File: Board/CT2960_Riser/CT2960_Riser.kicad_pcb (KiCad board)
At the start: 2 copper layers, 105 x 150 mm, 65 parts, among them IC1 74LVC8T245, IC2 74LVC8T245, IC3 74LVC8T245, IC4 74LVC8T245, IC5 74LVC8T245, IC6 74LVC8T245, J1 Conn_02x20_Odd_Even, J2 Conn_02x12_Top_Bottom, J3 Bus_ISA_16bit, J4 Conn_02x20_Odd_Even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

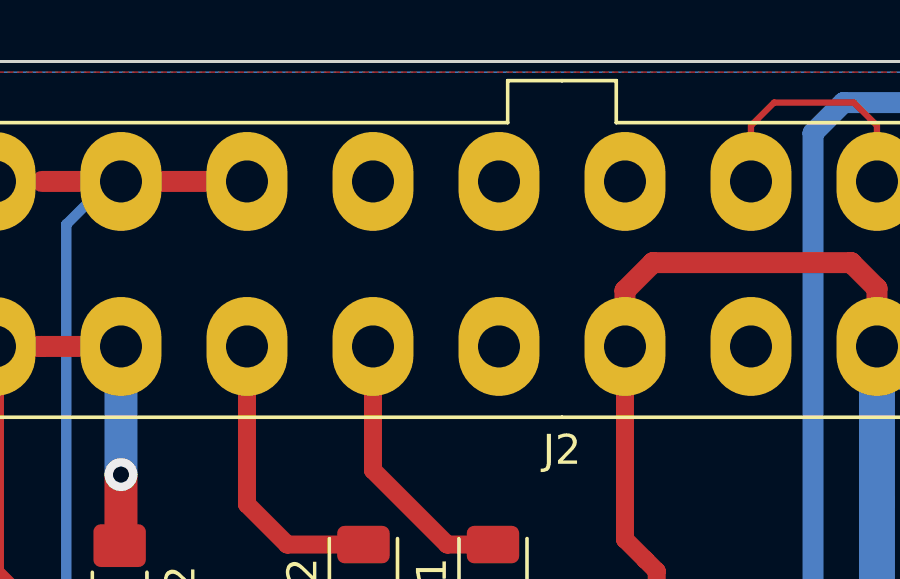
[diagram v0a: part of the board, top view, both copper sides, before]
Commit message: Fixed DRC from reporting unconnected trace/pad
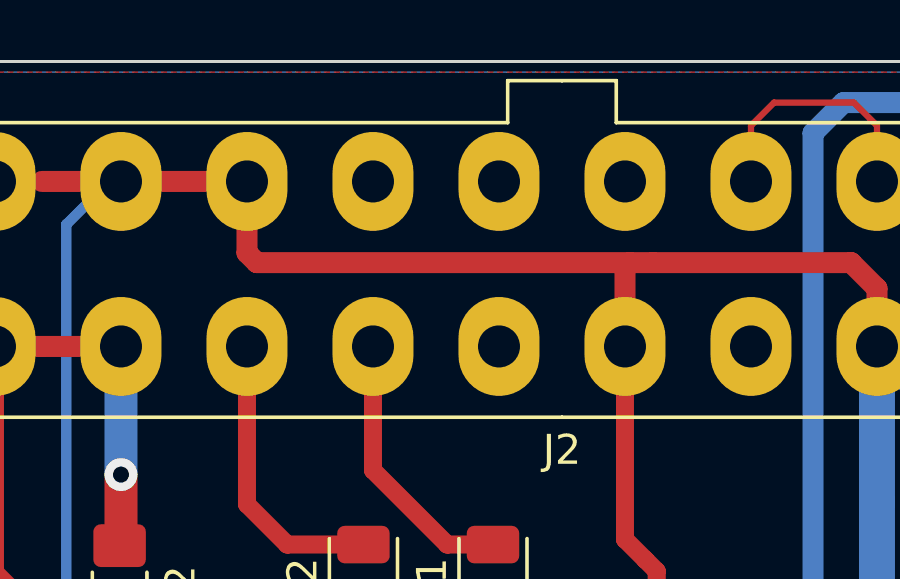
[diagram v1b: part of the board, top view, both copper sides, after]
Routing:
- net /ISA_VCC: track 502.2 -> 517.9 mm

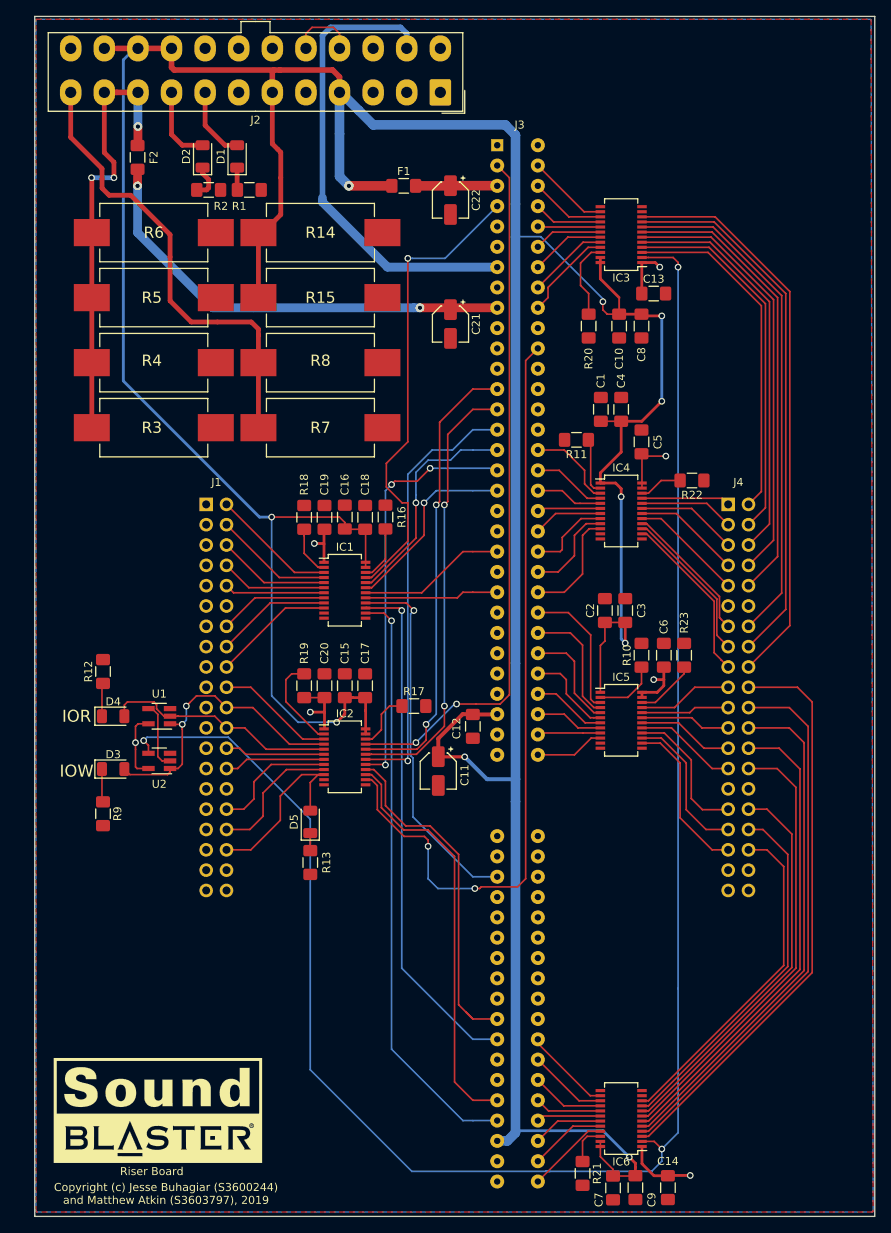
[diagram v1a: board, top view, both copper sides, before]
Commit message: Fixed up pin header location
It was off by a good 2mm... Fantastic for if you want to have it NOT fit
on top of the DE10....
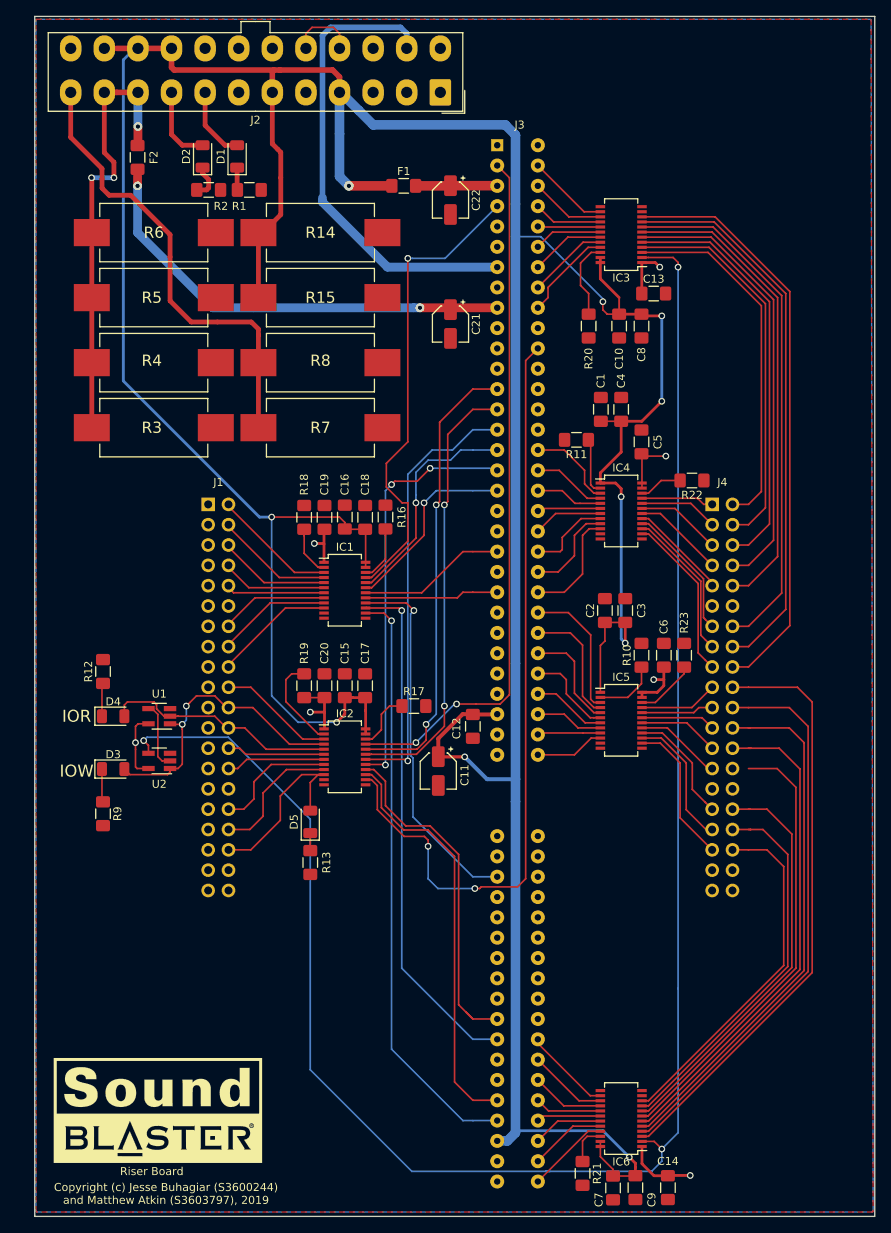
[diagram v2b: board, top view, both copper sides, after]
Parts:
- moved J4 2.00 mm to (157.7, 99.0)
- moved J1 0.25 mm to (94.7, 99.0)
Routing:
- net Net-(IC5-Pad16): track 17.6 -> 14.7 mm
- net Net-(IC5-Pad15): track 18.9 -> 16.2 mm
- net Net-(IC6-Pad9): track 45.7 -> 47.9 mm
- net Net-(IC6-Pad6): track 60.2 -> 62.5 mm
- net Net-(IC6-Pad8): track 49.6 -> 51.7 mm
- net Net-(IC6-Pad5): track 64.5 -> 66.7 mm
- net Net-(IC5-Pad14): track 20.3 -> 18.3 mm
- net Net-(IC5-Pad17): track 12.9 -> 10.9 mm
- net Net-(IC5-Pad19): track 11.3 -> 9.30 mm
- net Net-(IC6-Pad4): track 68.1 -> 70.1 mm
- net Net-(IC6-Pad3): track 72.3 -> 74.3 mm
- net Net-(IC6-Pad10): track 42.4 -> 44.4 mm
- net Net-(IC5-Pad21): track 11.8 -> 9.83 mm
- net Net-(IC5-Pad20): track 11.0 -> 9.04 mm
- net Net-(IC5-Pad18): track 12.1 -> 10.1 mm
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
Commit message: Commit 06052019
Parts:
- removed D3, D4: LED, LED_SMD:LED_1206_3216Metric
- added IOR: LED, LED_SMD:LED_1206_3216Metric, F.Cu at (126.7, 119.1)
- added IOW: LED, LED_SMD:LED_1206_3216Metric, F.Cu at (123.2, 119.1)
- C21, C22: footprint Capacitor_SMD:CP_Elec_4x5.8 -> Capacitor_SMD:CP_Elec_4x5.4
- R3, R4, R5, R6: value 39 -> 47
- R7, R8: value 6.8 -> 10
- moved R9 48.0 mm to (123.2, 113.8), turned to 90 degrees
- moved R12 45.6 mm to (126.7, 113.8)
- moved R7 8.13 mm to (108.7, 81.3), turned to 180 degrees
- moved R8 8.13 mm to (108.7, 89.4), turned to 180 degrees
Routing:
- net +3V3: track 110.5 -> 102.0 mm
- net Net-(IC2-Pad5): track 29.7 -> 21.4 mm
- net GND: track 8.56 -> 15.8 mm
- net Net-(IC2-Pad4): track 38.0 -> 31.3 mm
- net /IOR: track 55.4 -> 60.3 mm
- net Net-(IC6-Pad7): track 56.4 -> 60.5 mm
- net Net-(IC6-Pad3): track 74.3 -> 77.8 mm
- net Net-(IC6-Pad4): track 70.1 -> 73.6 mm
- net Net-(IC6-Pad5): track 66.7 -> 70.1 mm
- net Net-(IC6-Pad6): track 62.5 -> 65.8 mm
- net Net-(IC6-Pad8): track 51.7 -> 54.9 mm
- net Net-(IC6-Pad9): track 47.9 -> 51.0 mm
- net Net-(IC6-Pad10): track 44.4 -> 47.4 mm
- net +12V: track 112.5 -> 109.9 mm, vias 5 -> 3
- net /IOW: track 57.4 -> 59.3 mm, vias 2 -> 3
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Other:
- board text added: "Riser Board Rev 1.0a"
- board text removed: "IOR"
- board text removed: "IOW"
- board text removed: "Riser Board"
